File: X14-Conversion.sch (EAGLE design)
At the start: 34 parts, among them U2 LM2678

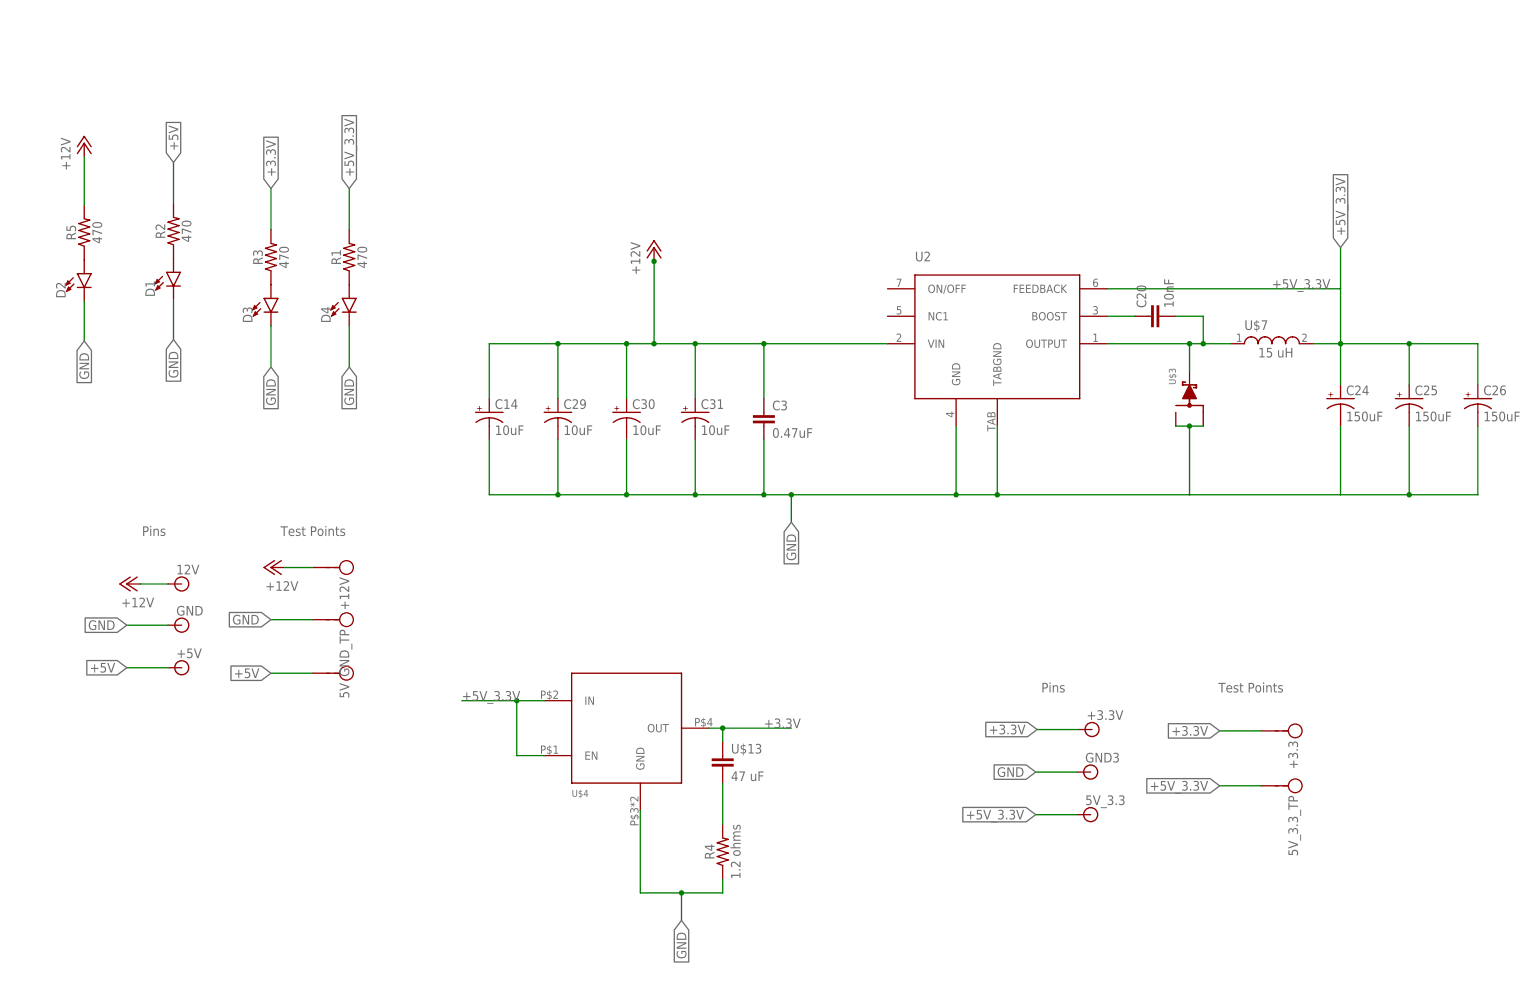
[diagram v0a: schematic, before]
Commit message: Added conversion board library
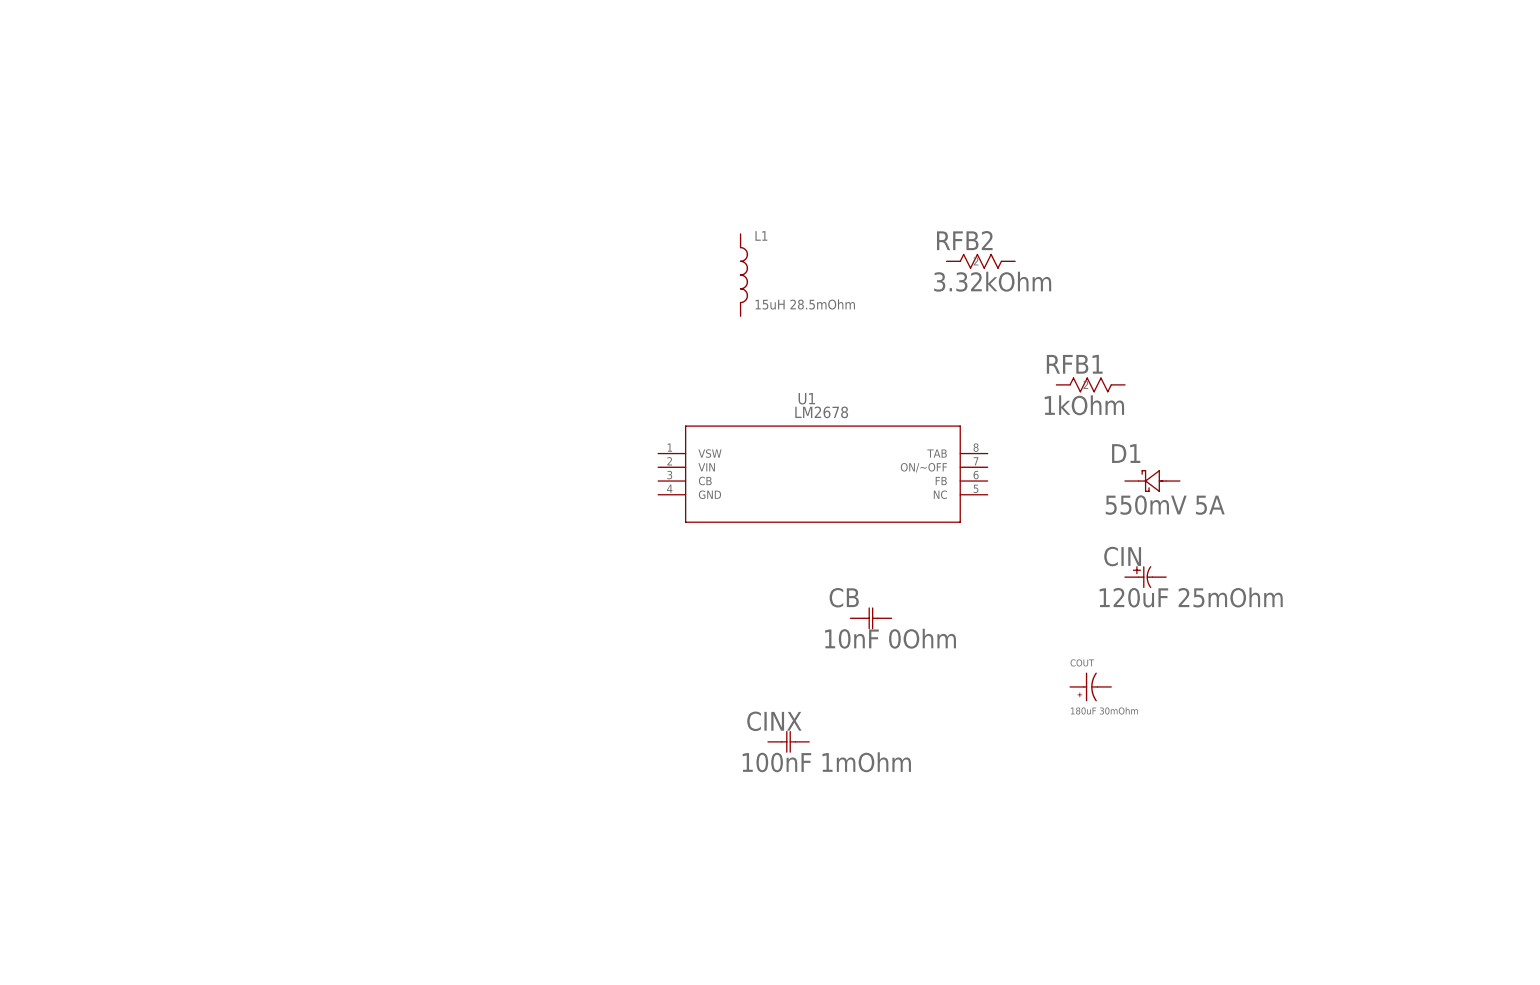
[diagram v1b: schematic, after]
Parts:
- removed +12V, +3.3, 5V, 5V_3.3_TP, GND_TP: TP, TP:TP
- removed +3.3V, +5V, 12V, 5V_3.3, GND, GND3: (no value), SparkFun-Connectors:BANANA_CONN
- removed C14, C29, C30, C31: 10uF, PowerComponents:C-TANTALUM(10UF_150UF)
- removed C20: 10nF, SparkFun-Capacitors:10NF-0603-50V-10%
- removed C24, C25, C26: 150uF, PowerComponents:C-TANTALUM(10UF_150UF)
- removed C3: 0.47uF, rcl:C-EUC0603
- removed D2, D3, D4: (no value), SparkFun-LED:LED0603
- removed R1, R2, R3, R5: 470, SparkFun-Resistors:470OHM-0603-1/10W-1%
- removed R4: 1.2 ohms, SparkFun-Resistors:RESISTOR0603
- removed U$13: 47 uF, Nordic_nRF:CAPACITOR_0603_N
- removed U$3: SWITCHMODE_SCHOTTKY, PowerComponents:SWITCHMODE_SCHOTTKY
- removed U$4: TO-263, TPS758:TO-263
- removed U$7: HCM1305, HCM1305:HCM1305
- removed U2: LM2678, PowerComponents:LM2678
- added CB: 10nF 0Ohm, CGA4C2C0G1H103J060AA:CGA4C2C0G1H103J060AACAP_2012_TDK
- added CIN: 120uF 25mOhm, 20SVPF120M:20SVPF120MPCAP_SVP_C6_PAN
- added CINX: 100nF 1mOhm, GRM155R71C104KA88D:GRM155R71C104KA88DCAP_GRM_155_MUR
- added COUT: 180uF 30mOhm, 16SVP180MX:16SVP180MX
- added L1: 15uH 28.5mOhm, IND, 15uH - hcma1305:HCMA1305
- added RFB1: 1kOhm, CRCW04021K00FKED:CRCW04021K00FKEDRES_CRCW_0402
- added RFB2: 3.32kOhm, CRCW04023K32FKED:CRCW04023K32FKEDRES_CRCW_0402
- added U1: LM2678, LM2678SX-ADJNOPB:LM2678SX-ADJ/NOPBTS7B
- D1: value (none) -> 550mV 5A; device SparkFun-LED:LED0603 -> CDBC520-G_Library:CDBC520-GCDBC-G
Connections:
- removed net +12V: +12V.P$1, 12V.1, C14.+, C29.+, C3.1, C30.+, C31.+, R5.2, U2.VIN
- removed net +3.3V: +3.3.P$1, +3.3V.1, R3.2, U$13.1, U$4.OUT
- removed net +5V: +5V.1, 5V.P$1, R2.2
- removed net +5V_3.3V: 5V_3.3.1, 5V_3.3_TP.P$1, C24.+, C25.+, C26.+, R1.2, U$4.EN, U$4.IN, U$7.2, U2.FEEDBACK
- removed net GND: C14.-, C24.-, C25.-, C26.-, C29.-, C3.2, C30.-, C31.-, D1.C, D2.C, D3.C, D4.C, GND.1, GND3.1, GND_TP.P$1, R4.1, U$3.P$1, U$3.P$3, U$4.GND, U2.GND, U2.TABGND
- removed net N$10: R4.2, U$13.2
- removed net N$2: C20.1, U2.BOOST
- removed net N$4: D2.A, R5.1
- removed net N$5: D3.A, R3.1
- removed net N$6: D4.A, R1.1
- removed net N$7: C20.2, U$3.P$4, U$7.1, U2.OUTPUT
- removed net N$8: D1.A, R2.1
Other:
- note removed: "Pins"
- note removed: "Test Points"

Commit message: Update new parts library
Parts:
- CB: value 10nF 0Ohm -> 10nF 0Ω
- CIN: value 120uF 25mOhm -> 120uF 25mΩ
- CINX: value 100nF 1mOhm -> 100nF 1mΩ
- COUT: value 180uF 30mOhm -> 180uF 30mΩ
- L1: value 15uH 28.5mOhm -> 15uH
- RFB1: value 1kOhm -> 1kΩ
- RFB2: value 3.32kOhm -> 3.32kΩ
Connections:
- new net GND: RFB1.1
- new net N$1: RFB1.2, RFB2.2, U1.FEEDBACK
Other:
- moved on the sheet: CB, CIN, CINX, COUT, D1, L1, RFB1, RFB2, U1

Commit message: Complete Schematic for LM2678
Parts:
- U1: value LM2678 -> LM2678SX-ADJ/NOPBTS7B
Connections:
- new net 12V: CIN.1, CINX.1, U1.VIN
- new net 5V: COUT.1, L1.2, RFB2.1
- new net N$2: CB.1, U1.CB
- new net N$3: CB.2, D1.1, L1.1, U1.SWITCH_OUTPUT
- net GND: now also CIN.2, CINX.2, COUT.2, D1.2, U1.GND
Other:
- moved on the sheet: CB, CIN, CINX, COUT, D1, L1, RFB1, RFB2

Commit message: Fix Schematic
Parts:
- added C1: 10uF 16V, CAP_GRM21BR61C106KE15L:GRM21BR61C106KE15L
- added C2: 22uF 16V, CAP_GRM21BR61C226ME44L:GRM21BR61C226ME44L
- added U$1: SOT150P410X160-3N, AZ1117C-3.3:SOT150P410X160-3N
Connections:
- new net 3.3V: C1.1, U$1.OUTPUT
- net 5V: now also C2.1, U$1.INPUT
- net GND: now also C1.2, C2.2, U$1.GND
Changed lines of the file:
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@@
 </classes>
 <parts>
-<part name="FRAME1" library="frames" library_urn="urn:adsk.eagle:library:229" deviceset="A3L-LOC" device=""/>
 <part name="RFB1" library="CRCW04021K00FKED" deviceset="CRCW04021K00FKED" device="RES_CRCW_0402" value="1kΩ"/>
 <part name="D1" library="CDBC520-G_Library" deviceset="CDBC520-G" device="CDBC-G" value="550mV 5A"/>
@@
 <part name="U1" library="LM2678SX-ADJNOPB" deviceset="LM2678SX-ADJ/NOPB" device="TS7B"/>
 <part name="GND2" library="supply1" library_urn="urn:adsk.eagle:library:371" deviceset="GND" device=""/>
-<part name="SUPPLY2" library="SparkFun-PowerSymbols" library_urn="urn:adsk.eagle:library:530" deviceset="5V" device=""/>
+<part name="SUPPLY2" library="SparkFun-PowerSymbols" library_urn="urn:adsk.eagle:library:530" deviceset="5V" device="" value="5.2V"/>
 <part name="SUPPLY1" library="SparkFun-PowerSymbols" library_urn="urn:adsk.eagle:library:530" deviceset="12V" device=""/>
+<part name="FRAME1" library="frames" library_urn="urn:adsk.eagle:library:229" deviceset="A3L-LOC" device=""/>
+<part name="U$1" library="AZ1117C-3.3" deviceset="SOT150P410X160-3N" device=""/>
+<part name="C1" library="CAP_GRM21BR61C106KE15L" deviceset="GRM21BR61C106KE15L" device="" value="10uF 16V"/>
+<part name="C2" library="CAP_GRM21BR61C226ME44L" deviceset="GRM21BR61C226ME44L" device="" value="22uF 16V"/>
+<part name="SUPPLY3" library="SparkFun-PowerSymbols" library_urn="urn:adsk.eagle:library:530" deviceset="5V" device="" value="5.2V"/>
+<part name="SUPPLY4" library="SparkFun-PowerSymbols" library_urn="urn:adsk.eagle:library:530" deviceset="3.3V" device=""/>
+<part name="GND3" library="supply1" library_urn="urn:adsk.eagle:library:371" deviceset="GND" device=""/>
+<part name="GND4" library="supply1" library_urn="urn:adsk.eagle:library:371" deviceset="GND" device=""/>
+<part name="GND5" library="supply1" library_urn="urn:adsk.eagle:library:371" deviceset="GND" device=""/>
 </parts>
 <sheets>
@@
 </plain>
 <instances>
-<instance part="FRAME1" gate="G$1" x="-157.48" y="-116.84" smashed="yes">
-<attribute name="DRAWING_NAME" x="186.69" y="-101.6" size="2.54" layer="94"/>
-<attribute name="LAST_DATE_TIME" x="186.69" y="-106.68" size="2.286" layer="94"/>
-<attribute name="SHEET" x="200.025" y="-111.76" size="2.54" layer="94"/>
-</instance>
 <instance part="RFB1" gate="A" x="40.64" y="73.66" smashed="yes">
 <attribute name="VALUE" x="44.6309" y="70.1421" size="1.27" layer="96" ratio="10"/>
@@
 </instance>
 <instance part="SUPPLY2" gate="G$1" x="81.534" y="44.958" smashed="yes" rot="R270">
-<attribute name="VALUE" x="84.582" y="46.228" size="1.778" layer="96" align="bottom-center"/>
+<attribute name="VALUE" x="88.138" y="44.196" size="1.778" layer="96" align="bottom-center"/>
 </instance>
 <instance part="SUPPLY1" gate="G$1" x="-56.134" y="50.038" smashed="yes" rot="R90">
 <attribute name="VALUE" x="-61.976" y="50.8" size="1.778" layer="96" rot="R180" align="bottom-center"/>
+</instance>
+<instance part="FRAME1" gate="G$1" x="-177.8" y="-116.84" smashed="yes">
+<attribute name="DRAWING_NAME" x="166.37" y="-101.6" size="2.54" layer="94"/>
+<attribute name="LAST_DATE_TIME" x="166.37" y="-106.68" size="2.286" layer="94"/>
+<attribute name="SHEET" x="179.705" y="-111.76" size="2.54" layer="94"/>
+</instance>
+<instance part="U$1" gate="G$1" x="-27.432" y="-25.908" smashed="yes"/>
+<instance part="C1" gate="G$1" x="0" y="-35.56" smashed="yes" rot="R270">
+<attribute name="NAME" x="-7.62" y="-36.82906875" size="1.77843125" layer="95"/>
+<attribute name="VALUE" x="-12.7" y="-43.18848125" size="1.78096875" layer="96"/>
+</instance>
+<instance part="C2" gate="G$1" x="-58.42" y="-38.1" smashed="yes" rot="R270">
+<attribute name="NAME" x="-55.88" y="-36.82906875" size="1.77843125" layer="95"/>
+<attribute name="VALUE" x="-55.88" y="-43.18848125" size="1.78096875" layer="96"/>
+</instance>
+<instance part="SUPPLY3" gate="G$1" x="-73.406" y="-25.654" smashed="yes" rot="R90">
+<attribute name="VALUE" x="-76.454" y="-26.924" size="1.778" layer="96" rot="R180" align="bottom-center"/>
+</instance>
+<instance part="SUPPLY4" gate="G$1" x="15.24" y="-25.654" smashed="yes" rot="R270">
+<attribute name="VALUE" x="17.78" y="-22.86" size="1.778" layer="96" align="bottom-center"/>
+</instance>
+<instance part="GND3" gate="1" x="-26.67" y="-50.8" smashed="yes">
+<attribute name="VALUE" x="-29.21" y="-53.34" size="1.778" layer="96"/>
+</instance>
+<instance part="GND4" gate="1" x="-58.42" y="-50.8" smashed="yes">
+<attribute name="VALUE" x="-60.96" y="-53.34" size="1.778" layer="96"/>
+</instance>
+<instance part="GND5" gate="1" x="0" y="-50.8" smashed="yes">
+<attribute name="VALUE" x="-2.54" y="-53.34" size="1.778" layer="96"/>
 </instance>
 </instances>
@@
 <junction x="-6.35" y="20.32"/>
 </segment>
+<segment>
+<pinref part="C2" gate="G$1" pin="2"/>
+<pinref part="GND4" gate="1" pin="GND"/>
+<wire x1="-58.42" y1="-43.18" x2="-58.42" y2="-48.26" width="0.1524" layer="91"/>
+</segment>
+<segment>
+<pinref part="U$1" gate="G$1" pin="GND"/>
+<pinref part="GND3" gate="1" pin="GND"/>
+<wire x1="-26.67" y1="-39.37" x2="-26.67" y2="-48.26" width="0.1524" layer="91"/>
+</segment>
+<segment>
+<pinref part="GND5" gate="1" pin="GND"/>
+<pinref part="C1" gate="G$1" pin="2"/>
+<wire x1="0" y1="-48.26" x2="0" y2="-40.64" width="0.1524" layer="91"/>
+</segment>
 </net>
 <net name="N$2" class="0">
@@
 <wire x1="81.534" y1="44.958" x2="66.294" y2="44.958" width="0.1524" layer="91"/>
 </segment>
+<segment>
+<pinref part="SUPPLY3" gate="G$1" pin="5V"/>
+<pinref part="U$1" gate="G$1" pin="INPUT"/>
+<wire x1="-73.406" y1="-25.654" x2="-58.42" y2="-25.654" width="0.1524" layer="91"/>
+<pinref part="C2" gate="G$1" pin="1"/>
+<wire x1="-58.42" y1="-25.654" x2="-43.18" y2="-25.654" width="0.1524" layer="91"/>
+<wire x1="-58.42" y1="-35.56" x2="-58.42" y2="-25.654" width="0.1524" layer="91"/>
+<junction x="-58.42" y="-25.654"/>
+</segment>
+</net>
+<net name="3.3V" class="0">
+<segment>
+<pinref part="U$1" gate="G$1" pin="OUTPUT"/>
+<pinref part="SUPPLY4" gate="G$1" pin="3.3V"/>
+<wire x1="-10.16" y1="-25.654" x2="0" y2="-25.654" width="0.1524" layer="91"/>
+<pinref part="C1" gate="G$1" pin="1"/>
+<wire x1="0" y1="-25.654" x2="15.24" y2="-25.654" width="0.1524" layer="91"/>
+<wire x1="0" y1="-33.02" x2="0" y2="-25.654" width="0.1524" layer="91"/>
+<junction x="0" y="-25.654"/>
+</segment>
 </net>
 </nets>
 </sheet>
 </sheets>
+<errors>
+</errors>
 </schematic>
 </drawing>

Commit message: Completing Schematic
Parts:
- added CONN: DISTRIBUTION-CONVERSION, CONN, Distribution-Conversion:DISTRIBUTION-CONVERSION
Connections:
- new net 5.2V: C2.1, COUT.1, L1.2, RFB2.1, U$1.INPUT
- net 12V: now also CONN.VIN+
- net 3.3V: now also CONN.VOUT+_3
- net 5V: now also CONN.VOUT+_5; no longer C2.1, COUT.1, L1.2, RFB2.1, U$1.INPUT
- net GND: now also CONN.VIN-, CONN.VOUT-
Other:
- note added: "Buck Controller 12V - 5.2V"
- note added: "Connectors to Power Distribution"
- note added: "Linear Regulator 5.2V - 3.3V"
- moved on the sheet: C1, C2, CB, CIN, CINX, COUT, D1, L1, RFB1, RFB2

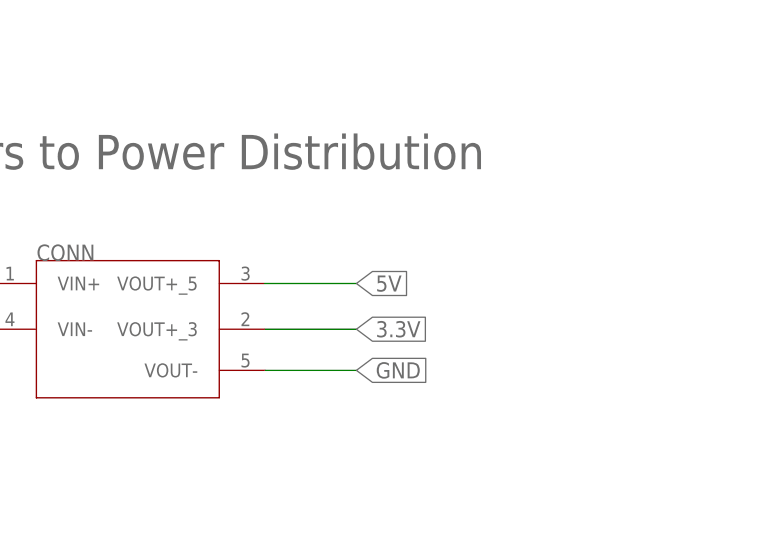
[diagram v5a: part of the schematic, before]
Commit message: Completing Schematic (1) and Upload Datasheets
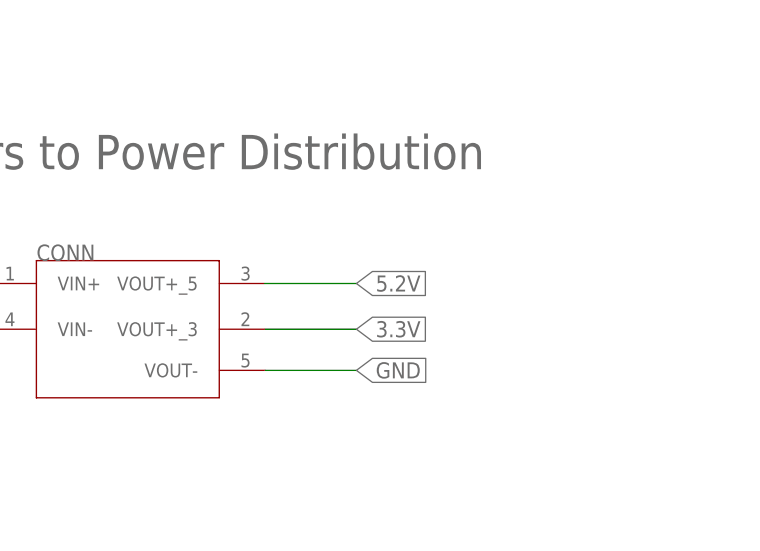
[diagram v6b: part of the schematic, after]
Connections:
- removed net 5V: CONN.VOUT+_5
- net 5.2V: now also CONN.VOUT+_5
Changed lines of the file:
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@@
-</segment>
-</net>
-<net name="5V" class="0">
-<segment>
-<pinref part="CONN" gate="G$1" pin="VOUT+_5"/>
-<wire x1="91.44" y1="-22.86" x2="101.6" y2="-22.86" width="0.1524" layer="91"/>
-<label x="101.6" y="-22.86" size="1.778" layer="95" xref="yes"/>
 </segment>
 </net>
@@
 <label x="-119.126" y="-18.034" size="1.778" layer="95" rot="R180" xref="yes"/>
 </segment>
+<segment>
+<pinref part="CONN" gate="G$1" pin="VOUT+_5"/>
+<wire x1="91.44" y1="-22.86" x2="101.6" y2="-22.86" width="0.1524" layer="91"/>
+<label x="101.6" y="-22.86" size="1.778" layer="95" xref="yes"/>
+</segment>
 </net>
